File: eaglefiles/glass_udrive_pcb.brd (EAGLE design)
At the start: 14.9 x 20 mm, 31 parts

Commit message: simple routing finish-up and silk-screen stuff.
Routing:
- net GLASS: track 1.68 -> 16.3 mm, vias 0 -> 1
- net BRG_BAL: track 0.00 -> 10.2 mm, vias 0 -> 2
- net CAP_COM: track 0.00 -> 6.04 mm, vias 0 -> 2
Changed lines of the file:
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@@
 </element>
 <element name="C2" library="GFL" package="0201" value="6800pF" x="8.1388" y="17.6896" smashed="yes" rot="R180">
-<attribute name="NAME" x="7.7488" y="18.1088" size="0.4" layer="25"/>
+<attribute name="NAME" x="7.3424" y="18.1088" size="0.4" layer="25"/>
 <attribute name="VALUE" x="8.7738" y="19.5946" size="1.27" layer="27" rot="R180"/>
 </element>
@@
 </element>
 <element name="C7" library="GFL" package="0603" value="10uF" x="8.1232" y="13.2764" smashed="yes" rot="R90">
-<attribute name="NAME" x="6.7358" y="13.165" size="0.508" layer="25" font="vector" rot="R270"/>
+<attribute name="NAME" x="8.971" y="13.3682" size="0.508" layer="25" font="vector" rot="R270"/>
 <attribute name="VALUE" x="9.698" y="12.0826" size="1.016" layer="27" font="vector" rot="R90"/>
 </element>
 <element name="C8" library="GFL" package="0603" value="10uF" x="14.6164" y="10.3656" smashed="yes" rot="R90">
-<attribute name="NAME" x="15.988" y="11.0514" size="0.508" layer="25" font="vector" rot="R90"/>
+<attribute name="NAME" x="13.7528" y="10.0354" size="0.508" layer="25" font="vector" rot="R90"/>
 <attribute name="VALUE" x="16.1912" y="9.1718" size="1.016" layer="27" font="vector" rot="R90"/>
 </element>
@@
 </element>
 <element name="C3" library="GFL" package="0201" value="6800pF" x="14.5288" y="14.7828" smashed="yes" rot="R180">
-<attribute name="NAME" x="14.7828" y="15.4432" size="0.508" layer="25" font="vector" rot="R180"/>
+<attribute name="NAME" x="14.478" y="14.5288" size="0.508" layer="25" font="vector" rot="R180"/>
 <attribute name="VALUE" x="15.7226" y="16.3576" size="1.016" layer="27" font="vector" rot="R180"/>
 </element>
@@
 <contactref element="OMNETICS" pad="V"/>
 <contactref element="CAPCOM" pad="2"/>
-<wire x1="8.262" y1="5.30489375" x2="10.2934" y2="2.6319" width="0" layer="19" extent="1-1"/>
+<wire x1="8.262" y1="5.30489375" x2="9.63030625" y2="5.30489375" width="0.1016" layer="1"/>
+<wire x1="9.63030625" y1="5.30489375" x2="9.652" y2="5.2832" width="0.1016" layer="1"/>
+<via x="9.652" y="5.2832" extent="1-16" drill="0.254"/>
+<wire x1="9.652" y1="5.2832" x2="9.8552" y2="5.2832" width="0.1016" layer="15"/>
+<wire x1="9.8552" y1="5.2832" x2="10.2616" y2="4.8768" width="0.1016" layer="15"/>
+<wire x1="10.2616" y1="4.8768" x2="10.2616" y2="1.8288" width="0.1016" layer="15"/>
+<via x="10.2616" y="1.8288" extent="1-16" drill="0.254"/>
+<wire x1="10.2616" y1="1.8288" x2="10.2616" y2="2.6001" width="0.1016" layer="1"/>
+<wire x1="10.2616" y1="2.6001" x2="10.2934" y2="2.6319" width="0.1016" layer="1"/>
 </signal>
 <signal name="STIM1_P">
@@
 <contactref element="OMNETICS" pad="B"/>
 <contactref element="BRIDGE" pad="2"/>
-<wire x1="7.079678125" y1="5.30709375" x2="12.1984" y2="2.6319" width="0" layer="19" extent="1-1"/>
+<wire x1="7.079678125" y1="5.30709375" x2="7.079678125" y2="4.909121875" width="0.1016" layer="1"/>
+<wire x1="7.079678125" y1="4.909121875" x2="7.2136" y2="4.7752" width="0.1016" layer="1"/>
+<wire x1="7.2136" y1="4.7752" x2="9.5504" y2="4.7752" width="0.1016" layer="1"/>
+<wire x1="9.5504" y1="4.7752" x2="9.7536" y2="4.572" width="0.1016" layer="1"/>
+<via x="9.7536" y="4.572" extent="1-16" drill="0.254"/>
+<wire x1="9.7536" y1="4.572" x2="9.7536" y2="1.524" width="0.1016" layer="15"/>
+<wire x1="9.7536" y1="1.524" x2="10.16" y2="1.2192" width="0.1016" layer="15"/>
+<wire x1="10.16" y1="1.2192" x2="12.0904" y2="1.2192" width="0.1016" layer="15"/>
+<wire x1="12.0904" y1="1.2192" x2="12.192" y2="1.3208" width="0.1016" layer="15"/>
+<via x="12.192" y="1.3208" extent="1-16" drill="0.254"/>
+<wire x1="12.192" y1="1.3208" x2="12.192" y2="2.6255" width="0.1016" layer="1"/>
+<wire x1="12.192" y1="2.6255" x2="12.1984" y2="2.6319" width="0.1016" layer="1"/>
 </signal>
 <signal name="I_COM">
@@
 <wire x1="8.5325" y1="17.6896" x2="8.5325" y2="17.9973" width="0.1016" layer="1"/>
 <wire x1="8.5325" y1="17.9973" x2="7.7866" y2="19.1464" width="0.1016" layer="1"/>
-<wire x1="8.262" y1="6.37169375" x2="8.5325" y2="17.6896" width="0" layer="19" extent="1-1"/>
-<wire x1="7.079678125" y1="6.37389375" x2="8.262" y2="6.37169375" width="0" layer="19" extent="1-1"/>
+<wire x1="7.079678125" y1="6.37389375" x2="7.081878125" y2="6.37169375" width="0.1016" layer="1"/>
+<wire x1="7.081878125" y1="6.37169375" x2="8.262" y2="6.37169375" width="0.1016" layer="1"/>
+<wire x1="8.262" y1="6.37169375" x2="8.262" y2="7.2828" width="0.1016" layer="1"/>
+<wire x1="8.262" y1="7.2828" x2="8.2296" y2="7.3152" width="0.1016" layer="1"/>
+<via x="8.2296" y="7.3152" extent="1-16" drill="0.254"/>
+<wire x1="8.2296" y1="7.3152" x2="8.2296" y2="10.4648" width="0.1016" layer="15"/>
+<wire x1="8.2296" y1="10.4648" x2="8.7376" y2="10.9728" width="0.1016" layer="15"/>
+<wire x1="8.7376" y1="10.9728" x2="8.7376" y2="18.1954" width="0.1016" layer="15"/>
+<wire x1="8.7376" y1="18.1954" x2="7.7866" y2="19.1464" width="0.1016" layer="15"/>
 </signal>
 <signal name="GLASS_OUT">

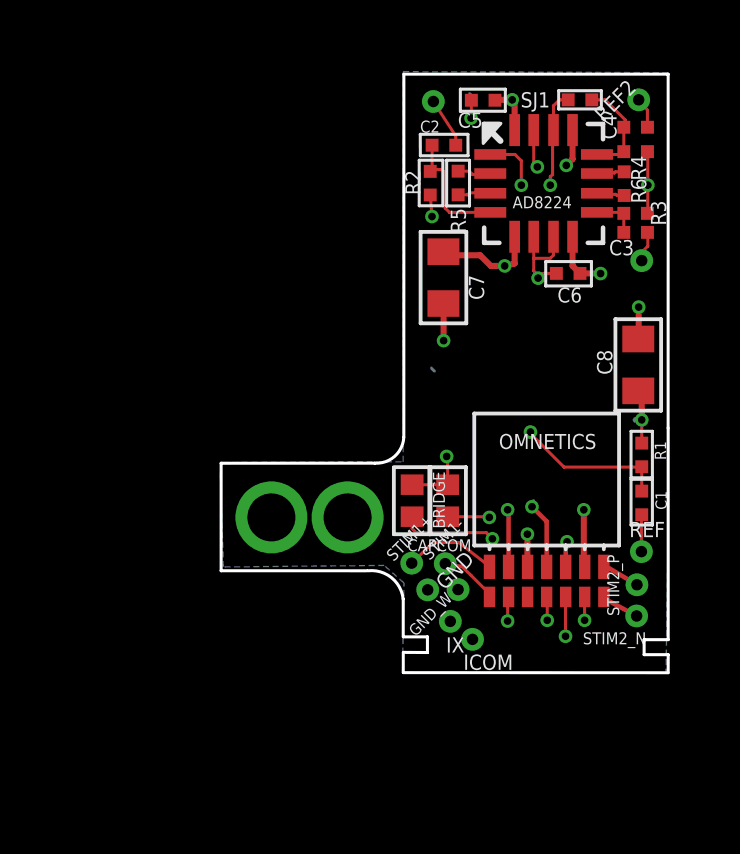
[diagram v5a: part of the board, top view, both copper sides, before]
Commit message: Went very OCD on your design
Made the power planes bigger because they had no reason not to be.

Renamed some nets because I found them confusing when looking at your schematic.

Moved stuff for cleaner routing.

Added a top ground plane to prevent stray capacitance onto any moving wires for
your electrode etc.

Improved via placement on bypass capacitors.

Re-organized schematic to some degree.

Renamed components to have more standard designator names, e.g. P1 instead of
'omnetics' and U1 instead of "AD82**"

Moved vias around to not make big breaks in the ground plane.

Messed with dimensions so they're all rectilinear and meet up with eachother.
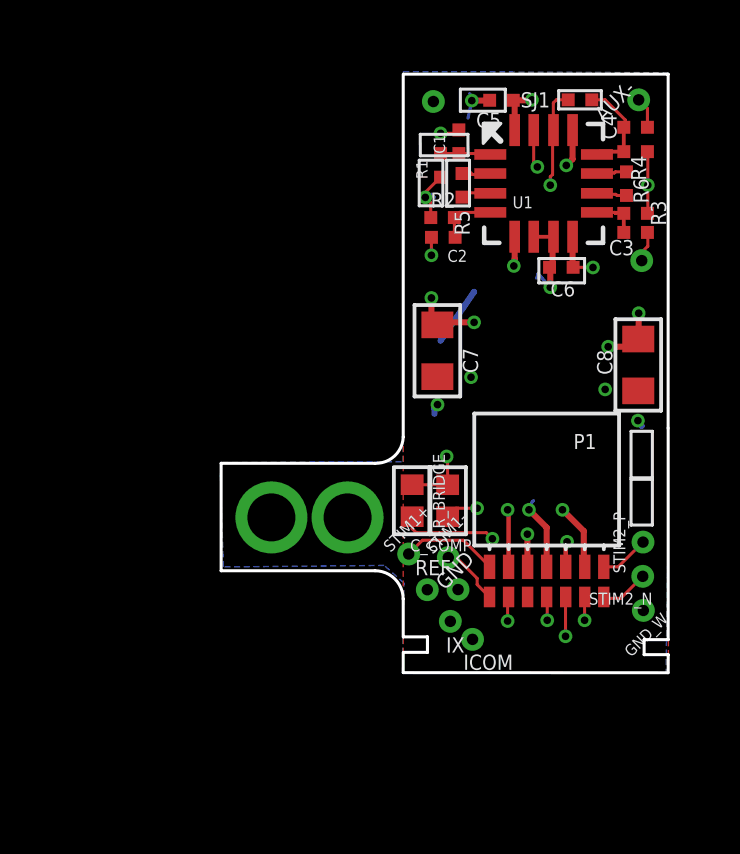
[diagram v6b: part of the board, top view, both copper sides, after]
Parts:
- SJ1: value (none) -> DNP
- moved C1 13.5 mm to (8.64, 17.8), turned to 270 degrees
- moved R1 11.8 mm to (8.03, 17.0), turned to 90 degrees
- moved REF 7.25 mm to (7.58, 2.87)
- moved GND_W 7.22 mm to (14.8, 2.18)
- moved C2 3.07 mm to (8.12, 14.6), turned to 0 degrees
- moved C7 2.45 mm to (7.92, 10.8)
- moved STIM2_P 1.44 mm to (14.8, 4.46)
- moved STIM2_N 1.34 mm to (14.8, 3.32)
- moved R2 1.22 mm to (8.09, 15.3), turned to 0 degrees
- moved C5 0.61 mm to (10.1, 19.2)
- moved STIM1+ 0.32 mm to (6.96, 4.06)
- moved C6 0.31 mm to (12.1, 13.6)
- moved STIM1- 0.23 mm to (8.28, 3.94)
- moved R5 0.15 mm to (8.74, 16.4)
- moved R6 0.08 mm to (14.2, 16.4)
- renumbered AD8224 to U1, BRIDGE to R_BRIDGE, CAPCOM to C_COMP, OMNETICS to P1, REF2 to AUX-, SIG2 to AUX+
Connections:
- net CHAN2_OUT renamed AUX_OUT
- net REF2 renamed AUX_N
- net REF_FLT2 renamed AUX_N_FLT
- net SIG2 renamed AUX_P
- net SIG2_FLT renamed AUX_P_FLT
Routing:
- net REF: track 1.23 -> 16.8 mm, vias 0 -> 1
- net REF_FLT: track 15.4 -> 1.67 mm, vias 2 -> 0
- net -15V: track 18.7 -> 21.2 mm, vias 4 -> 5
- net GLASS_FLT: track 4.12 -> 1.94 mm
- net +15V: track 16.4 -> 14.4 mm, vias 3 -> 5
- net GND: track 13.4 -> 15.2 mm, vias 9 -> 11
- net GLASS: track 16.3 -> 15.3 mm, vias 1 -> 2
- added copper zone on layer 1, net GND
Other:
- outline, holes or cut-outs redrawn

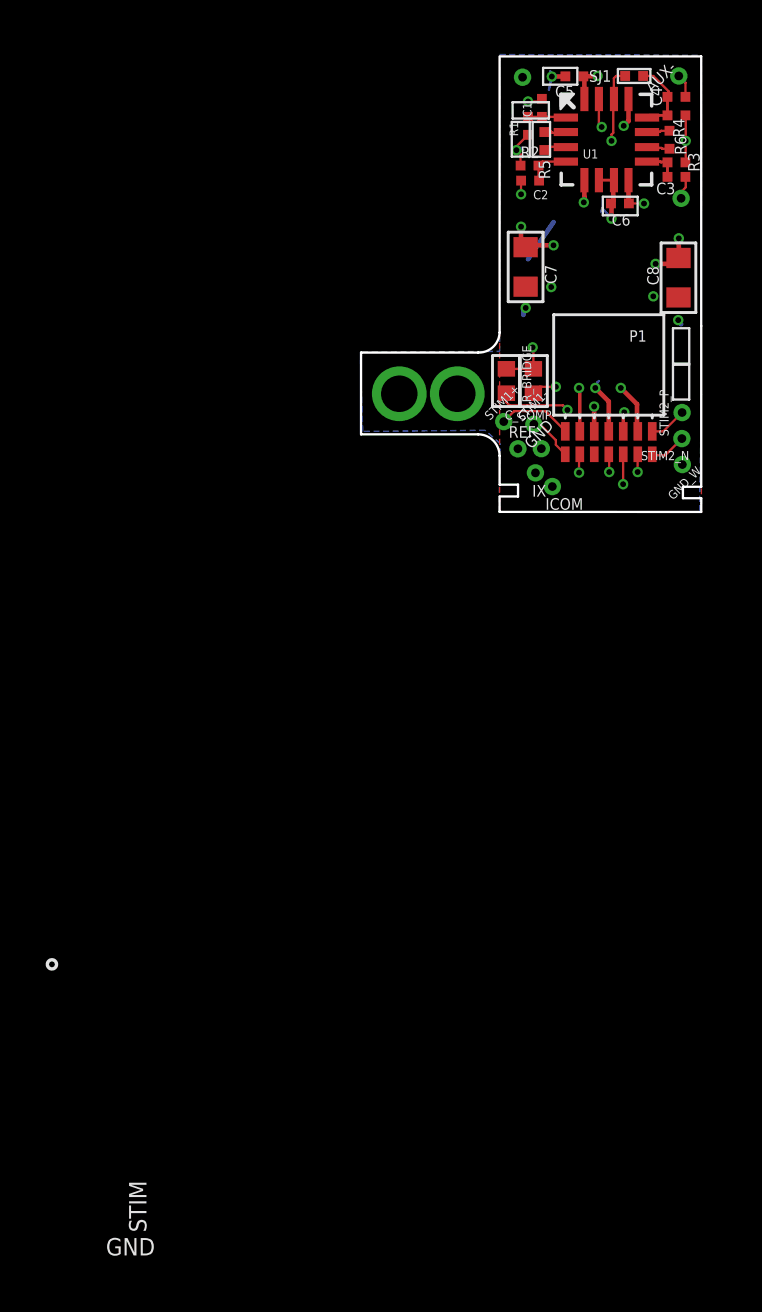
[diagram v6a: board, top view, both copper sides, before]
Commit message: Made glass net more compact.
Silk screen needs a lot of work
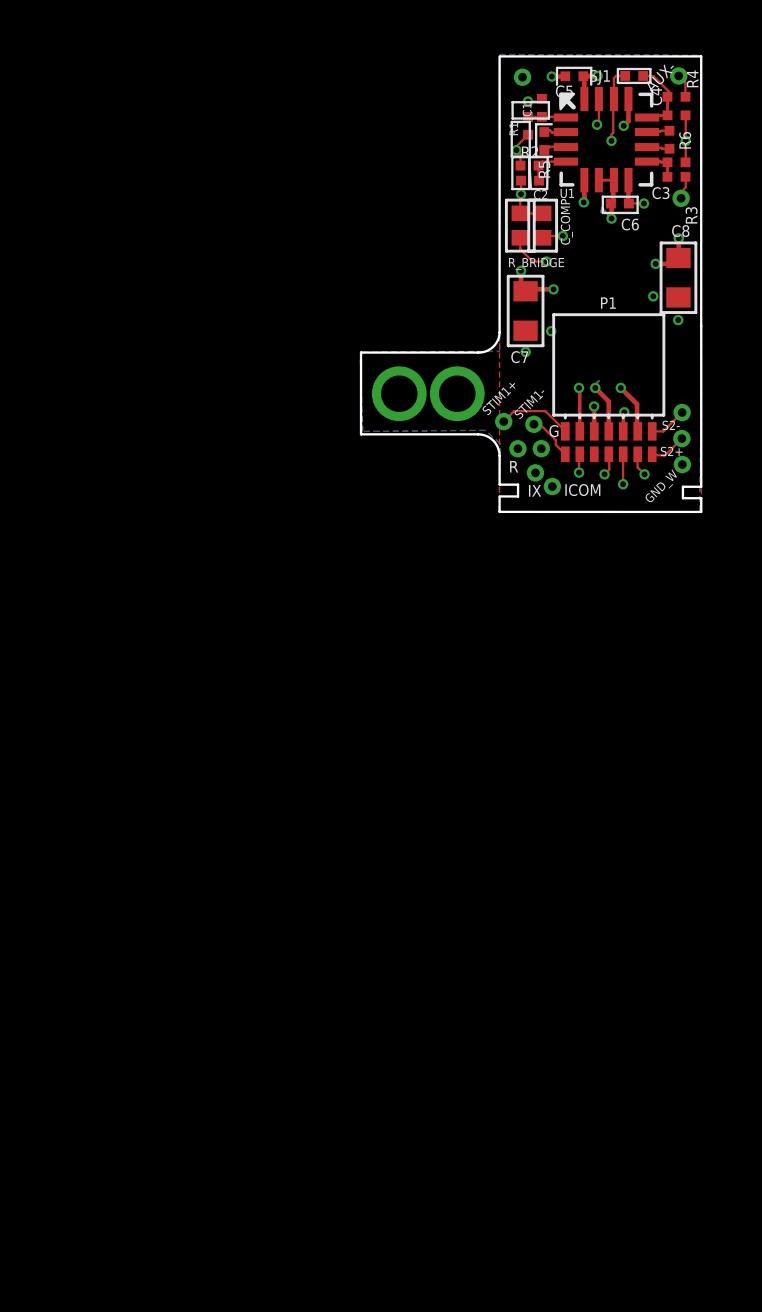
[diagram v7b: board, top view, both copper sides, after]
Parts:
- moved R_BRIDGE 6.83 mm to (7.69, 12.6)
- moved C_COMP 6.82 mm to (8.67, 12.6)
- moved C7 1.93 mm to (7.92, 8.91)
- renumbered GND to G, REF to R, STIM2_N to S2+, STIM2_P to S2-
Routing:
- net -15V: track 21.2 -> 10.4 mm
- net GLASS: track 15.3 -> 8.32 mm, vias 2 -> 1
- net CAP_COM: track 6.28 -> 12.8 mm
- net BRG_BAL: track 10.2 -> 16.1 mm
- net +15V: track 14.4 -> 8.46 mm
- net GND: track 15.2 -> 11.5 mm
- net I_COM: track 6.18 -> 5.62 mm
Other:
- board text removed: "GND"
- board text removed: "ICOM"
- board text removed: "STIM"

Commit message: improvements on slikscreen and component naming and placing.
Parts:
- renumbered GND_W to G_W
